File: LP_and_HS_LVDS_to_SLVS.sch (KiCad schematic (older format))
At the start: 2 parts

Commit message: Good, before replacing the swithches to TI ones
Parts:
- removed IC?: PI3WVR628XBEX, BGA24C40P4X6_170X240X50, symbol FMC_MIPI_v2:PI3WVR628XBEX
- added C21: 0.1uF, Capacitors_SMD:C_0402, symbol FMC_MIPI_v2:C
- added C22: 0.01uF, Capacitors_SMD:C_0402, symbol FMC_MIPI_v2:C
- added IC4: PI3WVR626XEBEX, QFN35P250X250X50-25N, symbol FMC_MIPI_v2:PI3WVR626XEBEX
- gave numbers to parts that had none: 1
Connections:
- net labels added: VOLT_2P5
- wire segments 84 -> 100
- no-connect marks 2 -> 0
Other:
- note added: "TODO: !!!\nCHECK IF THIS ONE IS Bi-DIRECTIONAL or at least will work in my setup!!!"

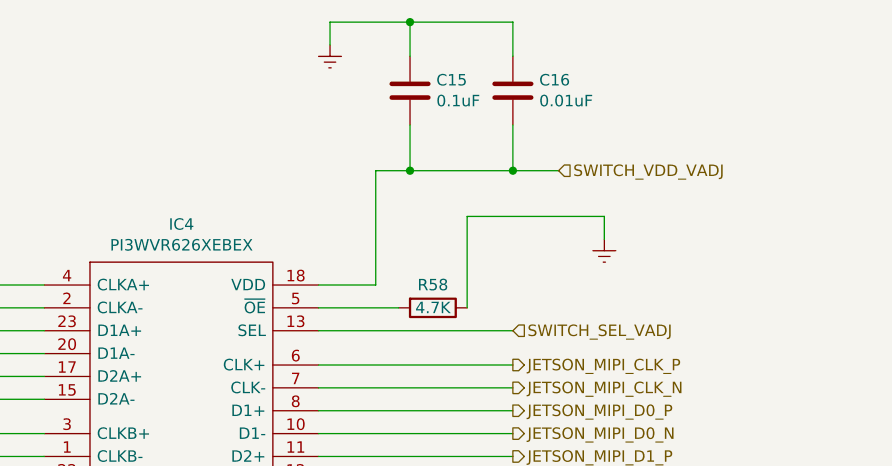
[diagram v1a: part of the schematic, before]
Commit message: good, added re-driver
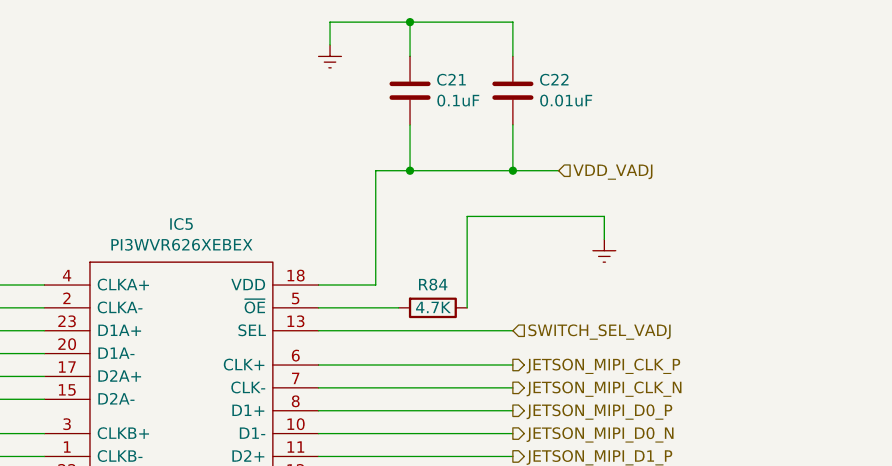
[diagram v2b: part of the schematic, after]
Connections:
- net SWITCH_VDD_VADJ renamed VDD_VADJ
